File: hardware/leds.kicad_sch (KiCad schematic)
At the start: 36 parts, among them J10 Conn_01x02, J11 Conn_01x02, J12 Conn_01x02, J13 Conn_01x02, J14 Conn_01x02, J5 Conn_01x02, J6 Conn_01x02, J7 Conn_01x02, J8 Conn_01x02, J9 Conn_01x02, Q10 AO3400A, Q11 AO3400A, Q12 AO3400A, Q3 AO3400A, Q4 AO3400A, Q5 AO3400A, Q6 AO3400A, Q7 AO3400A, Q8 AO3400A, Q9 AO3400A, U6 PCA9685PW

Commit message: clean up
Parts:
- renumbered C24 to C11, C25 to C12, C26 to C13, J11 to J10, J12 to J11, J13 to J12, J14 to J13, J5 to J4, J6 to J5, J7 to J6, J8 to J7, J9 to J8, J10 to J9, Q3 to Q1, Q12 to Q10, Q4 to Q2, Q5 to Q3, Q6 to Q4, Q7 to Q5, Q8 to Q6, Q9 to Q7, Q10 to Q8, Q11 to Q9, R28 to R14, R29 to R15, R30 to R16, R31 to R17, R32 to R18, R33 to R19, R34 to R20, R35 to R21, R36 to R22, R37 to R23, R38 to R24, R39 to R25, U6 to U4

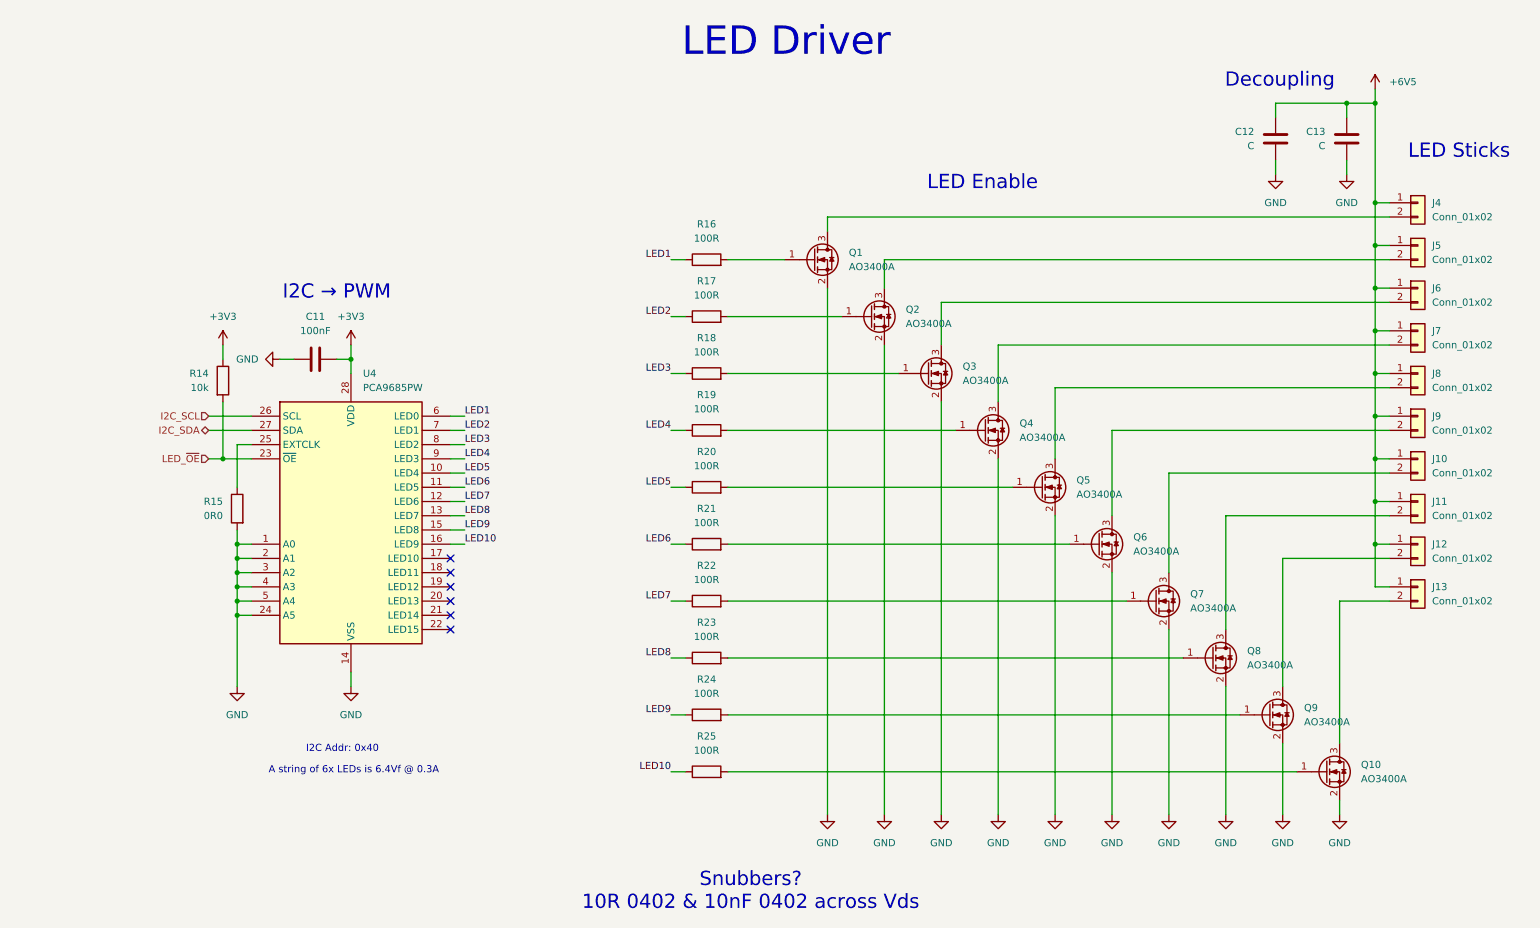
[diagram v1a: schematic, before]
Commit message: adding snubbers, starting placement
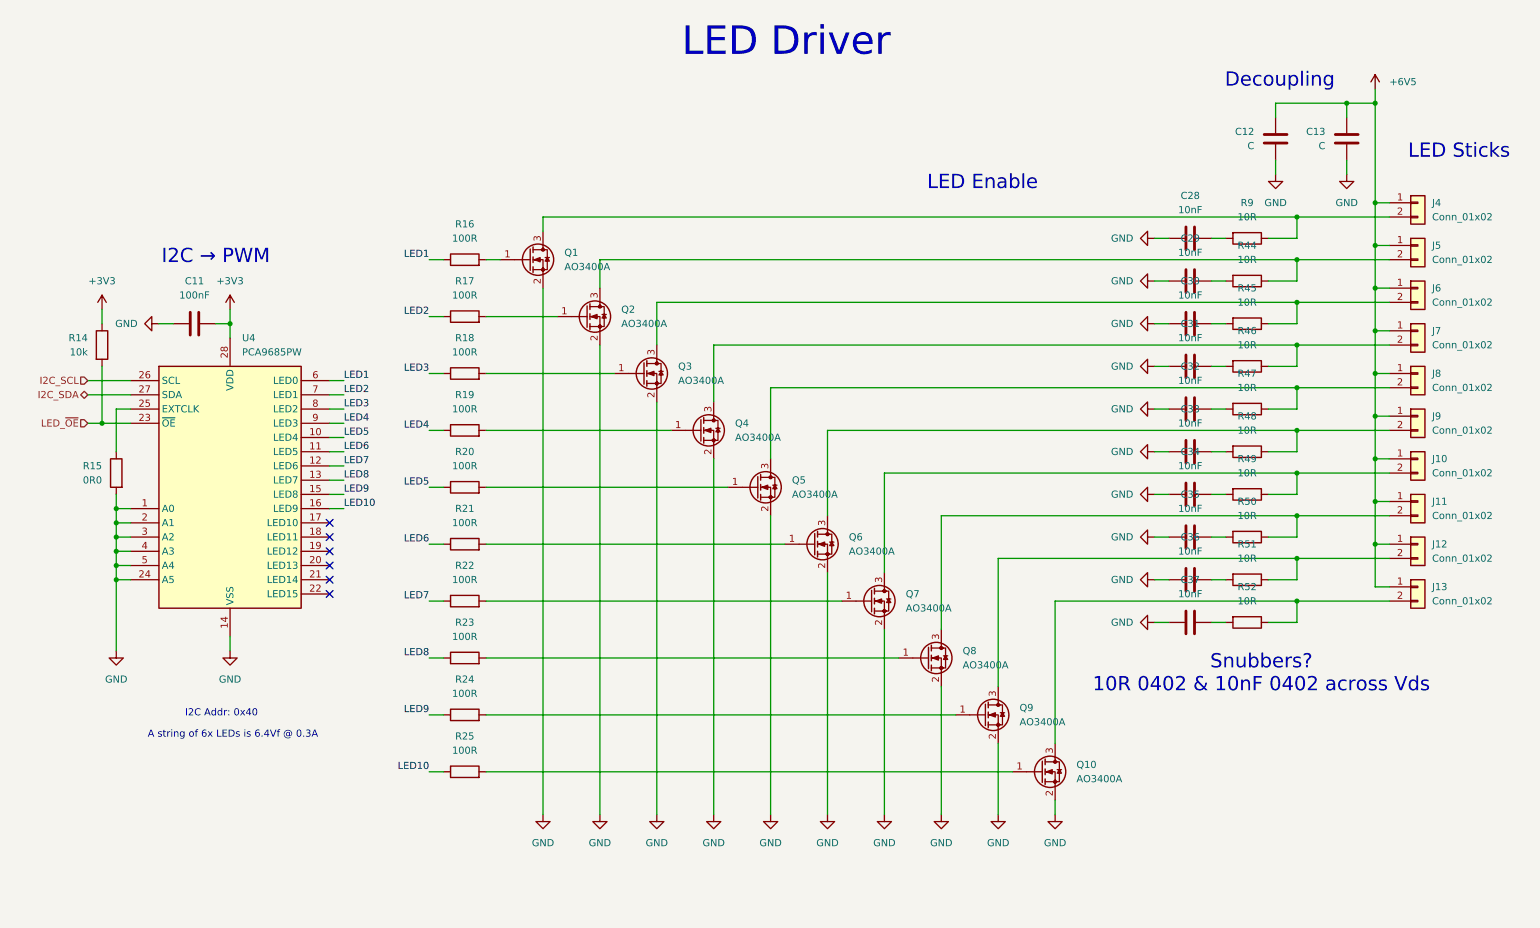
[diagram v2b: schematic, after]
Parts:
- added C28, C29, C30, C31, C32, C33, C34, C35, C36, C37: 10nF, Capacitor_SMD:C_0603_1608Metric, symbol Device:C
- added R44, R45, R46, R47, R48, R49, R50, R51, R52, R9: 10R, Resistor_SMD:R_0603_1608Metric, symbol Device:R
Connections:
- net GND: now also C28.1, C29.1, C30.1, C31.1, C32.1, C33.1, C34.1, C35.1, C36.1, C37.1
- net at J13.2 (Pin_2), Q10.3 (D): now also R52.1
- net at J5.2 (Pin_2), Q2.3 (D): now also R44.1
- net at J12.2 (Pin_2), Q9.3 (D): now also R51.1
- net at J7.2 (Pin_2), Q4.3 (D): now also R46.1
- net at J9.2 (Pin_2), Q6.3 (D): now also R48.1
- net at J4.2 (Pin_2), Q1.3 (D): now also R9.1
- net at J10.2 (Pin_2), Q7.3 (D): now also R49.1
- net at J11.2 (Pin_2), Q8.3 (D): now also R50.1
- net at J8.2 (Pin_2), Q5.3 (D): now also R47.1
- net at J6.2 (Pin_2), Q3.3 (D): now also R45.1
- new net: C37.2, R52.2
- new net: C36.2, R51.2
- new net: C28.2, R9.2
- new net: C34.2, R49.2
- new net: C32.2, R47.2
- new net: C33.2, R48.2
- new net: C35.2, R50.2
- new net: C30.2, R45.2
- new net: C31.2, R46.2
- new net: C29.2, R44.2
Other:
- moved on the sheet: C11, Q1, Q10, Q2, Q3, Q4, Q5, Q6, Q7, Q8, Q9, R14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

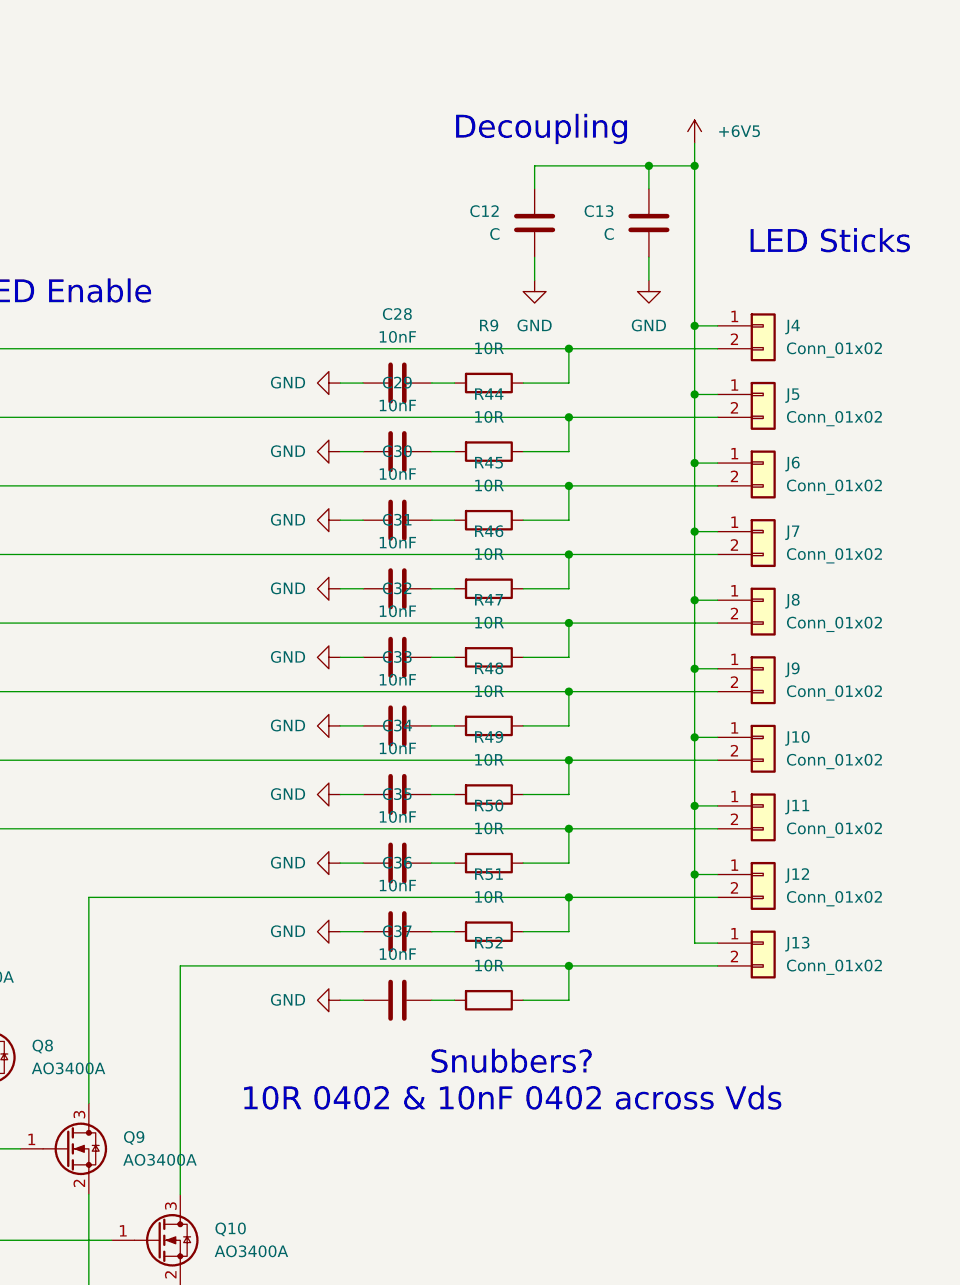
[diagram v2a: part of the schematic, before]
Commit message: updating PSUs
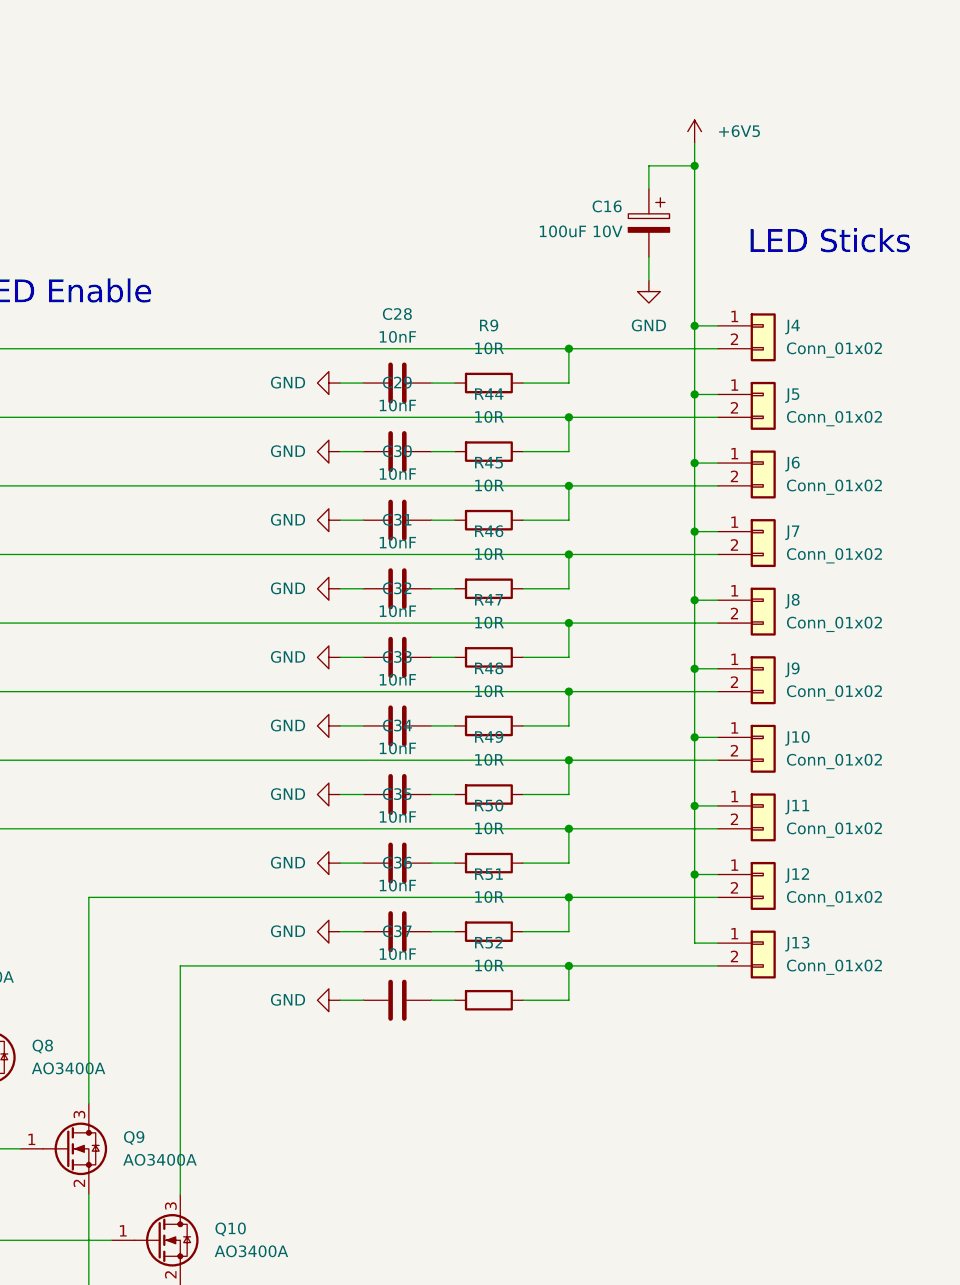
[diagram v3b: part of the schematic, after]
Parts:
- removed C12, C13: C, symbol Device:C
- added C16: 100uF 10V, symbol Device:C_Polarized
- C11: LCSC (none) -> C14663
- C28, C29, C30, C31, C32, C33, C34, C35, C36, C37: LCSC (none) -> C1589
- R14: LCSC (none) -> C21190
- R15: LCSC (none) -> C21189
- R16, R17, R18, R19, R20, R21, R22, R23, R24, R25: LCSC (none) -> C22775
- R44, R45, R46, R47, R48, R49, R50, R51, R52, R9: LCSC (none) -> C22859
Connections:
- net +6V5: now also C16.1
- net GND: now also C16.2
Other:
- note removed: "Decoupling"
- note removed: "Snubbers? 10R 0402 & 10nF 0402 across Vds"

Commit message: some jlc cleanup
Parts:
- C16: value 100uF 10V -> 100uF 16V; footprint (none) -> Capacitor_SMD:CP_Elec_6.3x7.7; LCSC (none) -> C72475
- C28, C29, C30, C31, C32, C33, C34, C35, C36, C37: LCSC C1589 -> C57112
- R14: LCSC C21190 -> C25804
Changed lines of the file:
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@@
 			)
 		)
-		(property "LCSC" "C1589"
+		(property "LCSC" "C57112"
 			(at 222.25 121.92 90)
 			(effects
@@
 			)
 		)
-		(property "LCSC" "C1589"
+		(property "LCSC" "C57112"
 			(at 222.25 53.34 90)
 			(effects
@@
 			)
 		)
-		(property "LCSC" "C21190"
+		(property "LCSC" "C25804"
 			(at 27.94 72.39 0)
 			(effects
@@
 			)
 		)
-		(property "LCSC" "C1589"
+		(property "LCSC" "C57112"
 			(at 222.25 83.82 90)
 			(effects
@@
 			)
 		)
-		(property "LCSC" "C1589"
+		(property "LCSC" "C57112"
 			(at 222.25 91.44 90)
 			(effects
@@
 			)
 		)
-		(property "LCSC" "C1589"
+		(property "LCSC" "C57112"
 			(at 222.25 106.68 90)
 			(effects
@@
 			)
 		)
-		(property "LCSC" "C1589"
+		(property "LCSC" "C57112"
 			(at 222.25 68.58 90)
 			(effects
@@
 			)
 		)
-		(property "LCSC" "C1589"
+		(property "LCSC" "C57112"
 			(at 222.25 114.3 90)
 			(effects
@@
 			)
 		)
-		(property "LCSC" "C1589"
+		(property "LCSC" "C57112"
 			(at 222.25 60.96 90)
 			(effects
@@
 			)
 		)
-		(property "LCSC" "C1589"
+		(property "LCSC" "C57112"
 			(at 222.25 99.06 90)
 			(effects
@@
 			)
 		)
-		(property "Value" "100uF 10V"
+		(property "Value" "100uF 16V"
 			(at 247.269 36.5376 0)
 			(effects
@@
 			)
 		)
-		(property "Footprint" ""
+		(property "Footprint" "Capacitor_SMD:CP_Elec_6.3x7.7"
 			(at 249.2248 39.37 0)
 			(effects
@@
 			)
 		)
+		(property "LCSC" "C72475"
+			(at 250.19 35.56 0)
+			(effects
+				(font
+					(size 1.27 1.27)
+				)
+				(hide yes)
+			)
+		)
 		(pin "1"
 		)
@@
 			)
 		)
-		(property "LCSC" "C1589"
+		(property "LCSC" "C57112"
 			(at 222.25 76.2 90)
 			(effects

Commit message: tweaking lcsc part numbers
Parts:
- C16: footprint Capacitor_SMD:CP_Elec_6.3x7.7 -> Capacitor_SMD:CP_Elec_6.3x5.7; LCSC C72475 -> C3646798
- U4: value PCA9685PW -> PCA9685PW,118; LCSC C92206 -> C2678753
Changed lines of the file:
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@@
 			)
 		)
-		(property "Value" "PCA9685PW"
+		(property "Value" "PCA9685PW,118"
 			(at 52.9433 73.66 0)
 			(effects
@@
 			)
 		)
-		(property "LCSC" "C92206"
+		(property "LCSC" "C2678753"
 			(at 50.8 96.52 0)
 			(effects
@@
 			)
 		)
-		(property "Footprint" "Capacitor_SMD:CP_Elec_6.3x7.7"
+		(property "Footprint" "Capacitor_SMD:CP_Elec_6.3x5.7"
 			(at 249.2248 39.37 0)
 			(effects
@@
 			)
 		)
-		(property "LCSC" "C72475"
+		(property "LCSC" "C3646798"
 			(at 250.19 35.56 0)
 			(effects

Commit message: general schematic and PCB clean
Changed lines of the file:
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@@
 	(text "LED Enable"
 		(exclude_from_sim no)
-		(at 185.166 43.434 0)
+		(at 155.194 44.958 0)
 		(effects
 			(font

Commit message: sorting button and LED
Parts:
- U4: Rotation Offset (none) -> 90
